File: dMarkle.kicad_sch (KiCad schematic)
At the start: 64 parts, among them SW1 SW_Choice, U1 74LS125, U10 INND-TS30RCB, U11 74LS125, U2 74HC4511, U3 Pico, U4 INND-TS30RCB, U5 74LS125, U6 74LS125, U7 74HC4511, U8 74HC4511, U9 INND-TS30RCB

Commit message: Rev 0.1
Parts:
- removed C11, C13, C15: 1u, Capacitor_THT:CP_Radial_D5.0mm_P2.00mm, symbol Device:C_Polarized_Small
- removed C12, C14, C16: 0u1, Capacitor_THT:C_Rect_L4.0mm_W2.5mm_P2.50mm, symbol Device:C_Small
- removed U1, U5, U6: 74LS125, Package_DIP:DIP-14_W7.62mm, symbol 74xx:74LS125
- removed U10, U9: INND-TS30RCB, Display_7Segment:HDSP-A151, symbol Display_Character:HDSP-A153
- removed U7, U8: 74HC4511, Package_DIP:DIP-16_W7.62mm, symbol CustomParts:74HC4511
- added D3, D4: INND-TS30RCB, Display_7Segment:HDSP-A151, symbol Display_Character:HDSP-A153
- added Q1: 2N7000, Package_TO_SOT_THT:TO-92_Inline, symbol Transistor_FET:2N7000
- added R7: 10k, Resistor_THT:R_Axial_DIN0204_L3.6mm_D1.6mm_P5.08mm_Horizontal, symbol Device:R_Small
- added SW2: SW_EN, Button_Switch_THT:SW_CuK_OS102011MA1QN1_SPDT_Angled, symbol Switch:SW_SPDT
- added U3, U4: 74HC4511, Package_DIP:DIP-16_W7.62mm, symbol CustomParts:74HC4511
- C1, C3: footprint Capacitor_THT:CP_Radial_D5.0mm_P2.00mm -> Capacitor_THT:C_Rect_L4.0mm_W2.5mm_P2.50mm; symbol Device:C_Polarized_Small -> Device:C_Small
- C5: renamed from C6; footprint Capacitor_THT:CP_Radial_D5.0mm_P2.00mm -> Capacitor_THT:C_Rect_L4.0mm_W2.5mm_P2.50mm; symbol Device:C_Polarized_Small -> Device:C_Small
- C7: renamed from C9; footprint Capacitor_THT:CP_Radial_D5.0mm_P2.00mm -> Capacitor_THT:C_Rect_L4.0mm_W2.5mm_P2.50mm; symbol Device:C_Polarized_Small -> Device:C_Small
- renumbered C8 to C10, C17 to C11, C18 to C12, C19 to C13, C7 to C6, C10 to C8, C5 to C9, U4 to D2, R9 to R10, R8 to R11, R7 to R12, R12 to R14, R14 to R29, R11 to R8, R10 to R9, U3 to U1, U11 to U5
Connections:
- net DIG0_0 is gone; now on net D0: U1.1 (GPIO0)
- net DIG0_1 is gone; now on net D1: U1.2 (GPIO1)
- net DIG0_2 is gone; now on net D2: U1.4 (GPIO2)
- net DIG0_3 is gone; now on net D3: U1.5 (GPIO3)
- net +3.3V: now also C1.1, C2.1, C3.1, C4.1, C5.1, C6.1, C7.1, C8.1, D1.2 (A), U2.16 (VCC), U2.3 (~{LT}), Q1.2 (G), R7.1, SW2.3 (C), U3.16 (VCC), U3.3 (~{LT}), U4.16 (VCC), U4.3 (~{LT})
- net +5V: now also Q1.3 (D); no longer C1.1, C2.1, C3.1, C4.1, C5.1, C6.1, C7.1, C8.1, D1.2 (A), U2.16 (VCC), U2.3 (~{LT}), U2.4 (~{BL})
- net GND: now also D3.1 (CC), D3.6 (CC), D4.1 (CC), D4.6 (CC), Q1.1 (S), R7.2, SW2.1 (A), U3.8 (GND), U4.8 (GND); no longer U2.5 (~{LE})
- net D1: now reaches U2.1 (D1)
- net D1: now also U3.1 (D1), U4.1 (D1)
- net D2: now reaches U2.2 (D2)
- net D2: now also U3.2 (D2), U4.2 (D2)
- net D3: now reaches U2.6 (D3)
- net D3: now also U3.6 (D3), U4.6 (D3)
- net D0: now reaches U2.7 (D0)
- net D0: now also U3.7 (D0), U4.7 (D0)
- net ENABLE: now reaches U1.37 (3V3_EN)
- net ENABLE: now also SW2.2 (B)
- net ~{BL}1: now reaches U1.6 (GPIO4)
- net ~{BL}1: now also U2.4 (~{BL})
- net ~{BL}2: now reaches U1.7 (GPIO5)
- net ~{BL}2: now also U3.4 (~{BL})
- net D1A: no longer names the net of R12.1, U2.13 (a)
- net D1Ar: no longer names the net of D2.10 (A), R12.2
- net D1B: no longer names the net of R11.1, U2.12 (b)
- net D1Br: no longer names the net of D2.9 (B), R11.2
- net D1C: no longer names the net of R10.1, U2.11 (c)
- net D1Cr: no longer names the net of D2.8 (C), R10.2
- net D1D: no longer names the net of R9.1, U2.10 (d)
- net D1Dr: no longer names the net of D2.5 (D), R9.2
- net D1E: no longer names the net of R8.1, U2.9 (e)
- net D1Er: no longer names the net of D2.4 (E), R8.2
- net D1F: no longer names the net of R14.1, U2.15 (f)
- net D1Fr: no longer names the net of D2.2 (F), R14.2
- net D1G: no longer names the net of R13.1, U2.14 (g)
- net D1Gr: no longer names the net of D2.3 (G), R13.2
- net D2A: no longer names the net of R15.1
- net D2A: now also U3.9 (e)
- net D2Ar: no longer names the net of R15.2
- net D2Ar: now also D3.4 (E)
- net D2B: no longer names the net of R16.1
- net D2B: now also U3.10 (d)
- net D2Br: no longer names the net of R16.2
- net D2Br: now also D3.5 (D)
- net D2C: no longer names the net of R17.1
- net D2C: now also U3.11 (c)
- net D2Cr: no longer names the net of R17.2
- net D2Cr: now also D3.8 (C)
- net D2D: no longer names the net of R18.1
- net D2D: now also U3.12 (b)
- net D2Dr: no longer names the net of R18.2
- net D2Dr: now also D3.9 (B)
- net D2E: no longer names the net of R19.1
- net D2E: now also U3.13 (a)
- net D2Er: no longer names the net of R19.2
- net D2Er: now also D3.10 (A)
- net D2F: no longer names the net of R20.1
- net D2F: now also U3.14 (g)
- net D2Fr: no longer names the net of R20.2
- net D2Fr: now also D3.3 (G)
- net D2G: no longer names the net of R21.1
- net D2G: now also U3.15 (f)
- net D2Gr: no longer names the net of R21.2
- net D2Gr: now also D3.2 (F)
- net D3A: no longer names the net of R22.1
- net D3A: now also U4.9 (e)
- net D3Ar: no longer names the net of R22.2
- net D3Ar: now also D4.4 (E)
- net D3B: no longer names the net of R23.1
- net D3B: now also U4.10 (d)
- net D3Br: no longer names the net of R23.2
- net D3Br: now also D4.5 (D)
- net D3C: no longer names the net of R24.1
- net D3C: now also U4.11 (c)
- net D3Cr: no longer names the net of R24.2
- net D3Cr: now also D4.8 (C)
- net D3D: no longer names the net of R25.1
- net D3D: now also U4.12 (b)
- net D3Dr: no longer names the net of R25.2
- net D3Dr: now also D4.9 (B)
- net D3E: no longer names the net of R26.1
- net D3E: now also U4.13 (a)
- net D3Er: no longer names the net of R26.2
- net D3Er: now also D4.10 (A)
- net D3F: no longer names the net of R27.1
- net D3F: now also U4.14 (g)
- net D3Fr: no longer names the net of R27.2
- net D3Fr: now also D4.3 (G)
- net D3G: no longer names the net of R28.1
- net D3G: now also U4.15 (f)
- net D3Gr: no longer names the net of R28.2
- net D3Gr: now also D4.2 (F)
- net DIG1_0 renamed ~{BL}3
- net ~{BL}3: now also U4.4 (~{BL})
- net DIG1_1 renamed ~{LE}1
- net ~{LE}1: now also U2.5 (~{LE})
- net DIG1_2 renamed ~{LE}2
- net ~{LE}2: now also U3.5 (~{LE})
- net DIG1_3 renamed ~{LE}3
- net ~{LE}3: now also U4.5 (~{LE})
- net DIG2_0: no longer names the net of U1.14 (GPIO10)
- net DIG2_1: no longer names the net of U1.15 (GPIO11)
- net DIG2_2: no longer names the net of U1.16 (GPIO12)
- net DIG2_3: no longer names the net of U1.17 (GPIO13)
- no-connect marks 22 -> 23
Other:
- note removed: "3V3 to 5V BCD 7-Segment Display Logic"
- moved on the sheet: C10, C11, C9, D2, R1, R10, R11, R12, R13, R14, R2, R3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

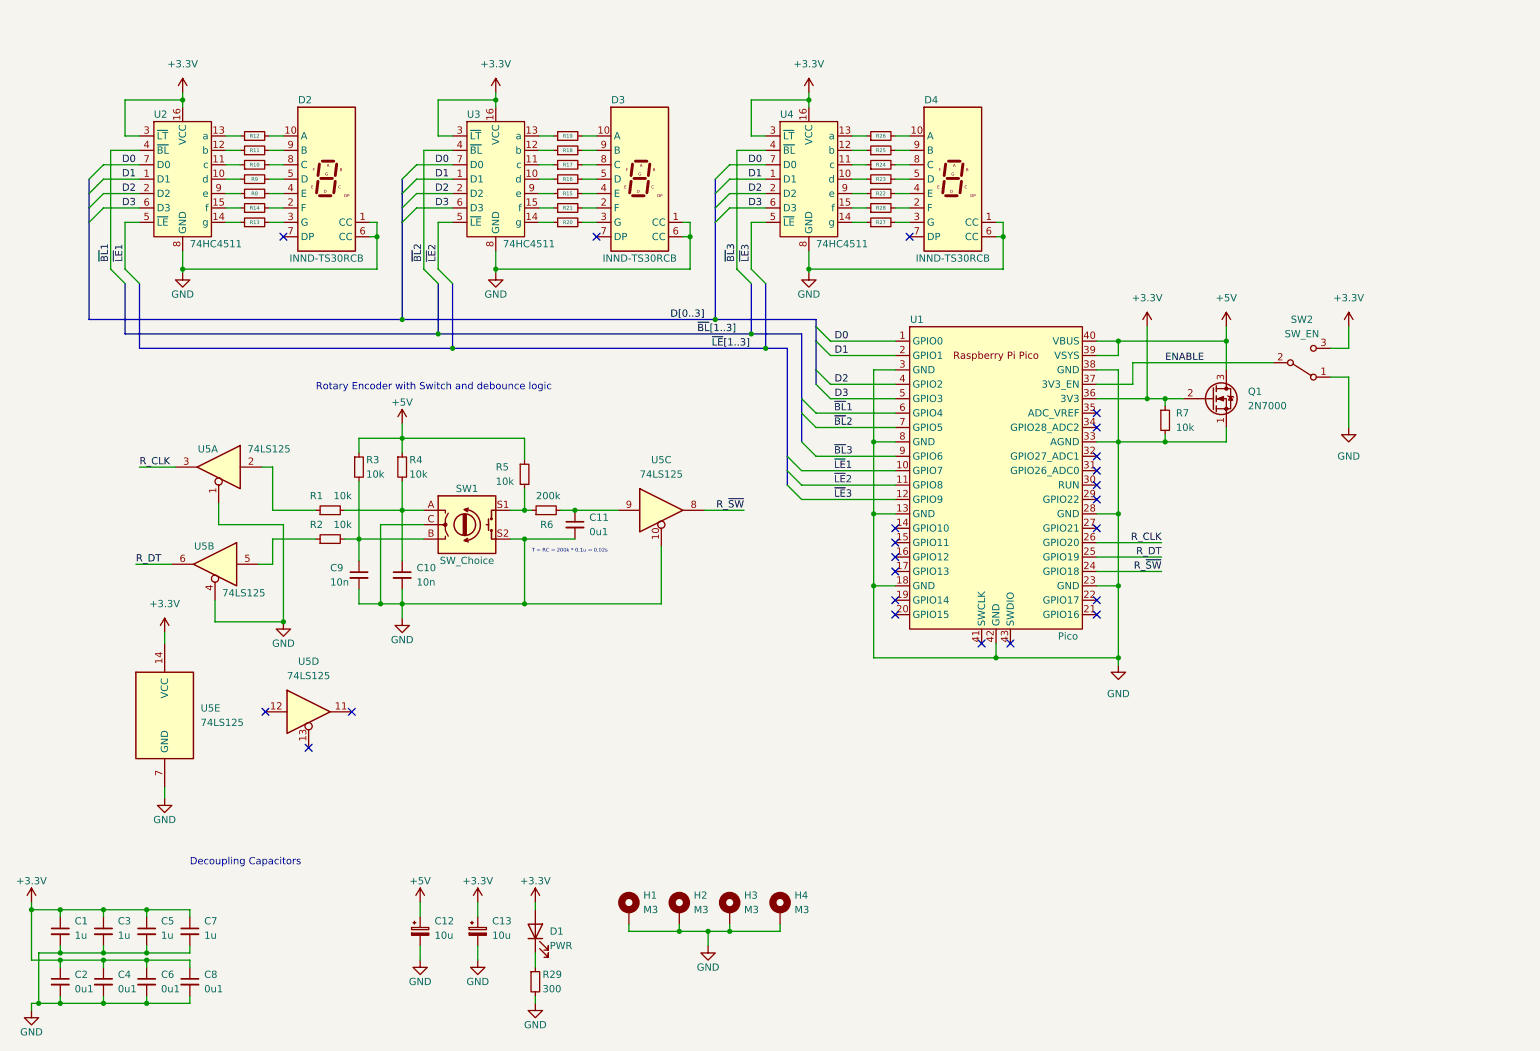
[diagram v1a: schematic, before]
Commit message: All 5V usage removed. Rev0.1 complete.
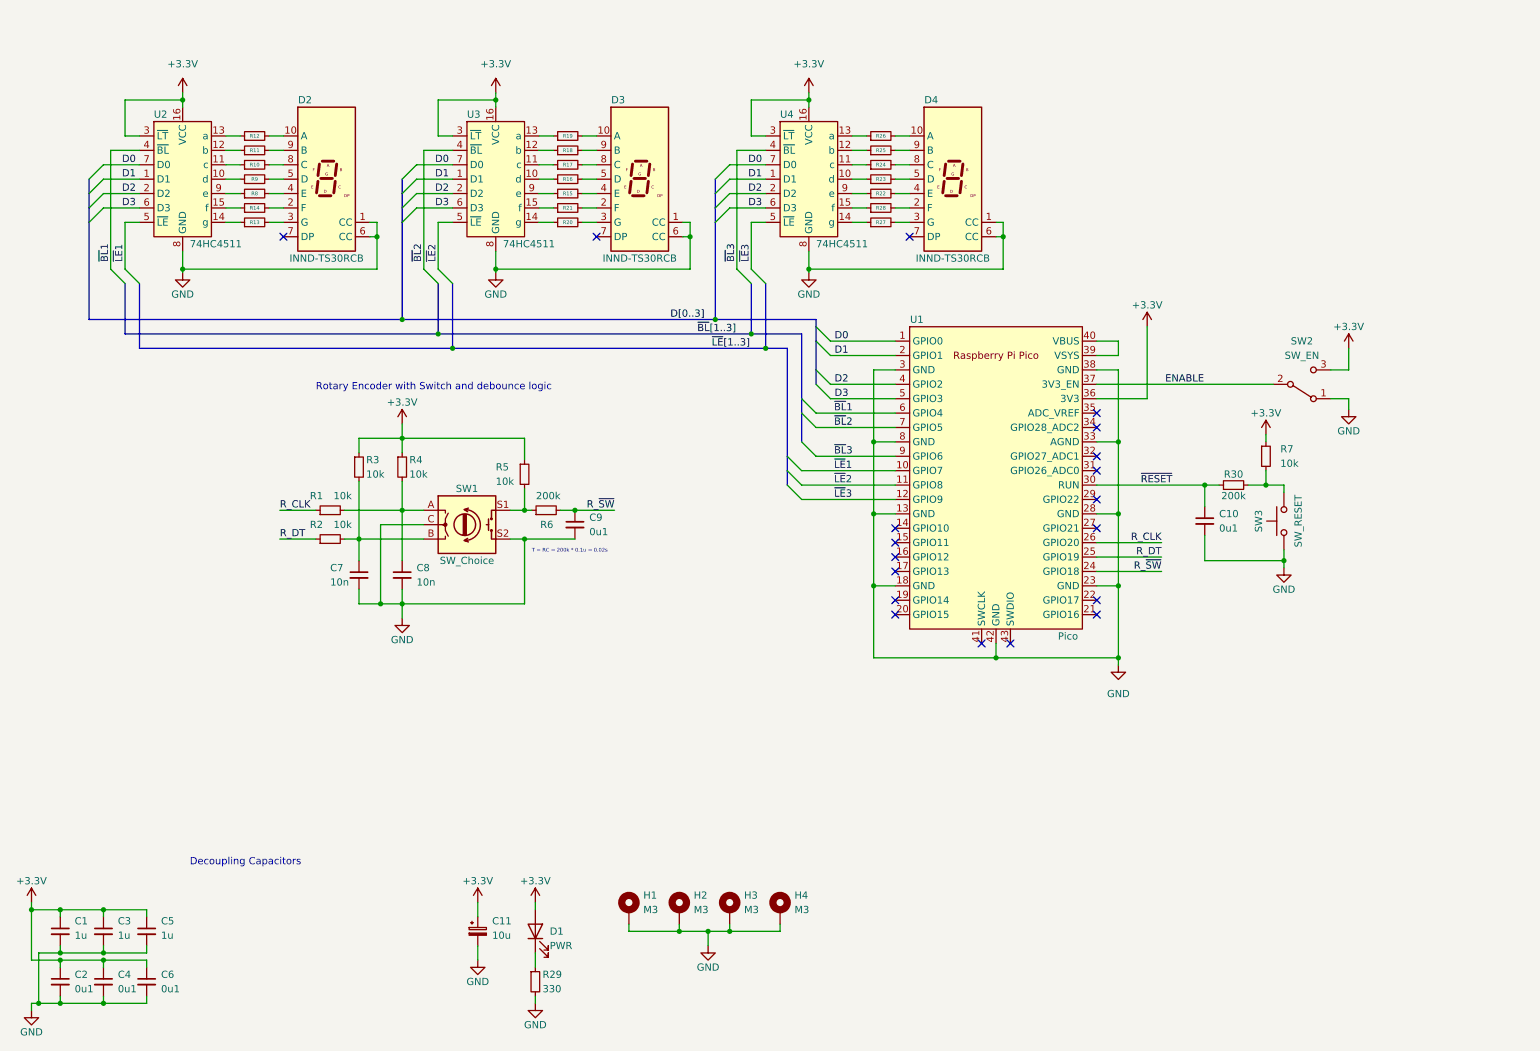
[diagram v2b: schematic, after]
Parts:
- removed C12: 10u, Capacitor_THT:CP_Radial_D5.0mm_P2.00mm, symbol Device:C_Polarized_Small
- removed C7: 1u, Capacitor_THT:C_Rect_L4.0mm_W2.5mm_P2.50mm, symbol Device:C_Small
- removed C8: 0u1, Capacitor_THT:C_Rect_L4.0mm_W2.5mm_P2.50mm, symbol Device:C_Small
- removed Q1: 2N7000, Package_TO_SOT_THT:TO-92_Inline, symbol Transistor_FET:2N7000
- removed U5: 74LS125, Package_DIP:DIP-14_W7.62mm, symbol 74xx:74LS125
- added C10: 0u1, Capacitor_THT:C_Rect_L4.0mm_W2.5mm_P2.50mm, symbol Device:C_Small
- added R30: 200k, Resistor_THT:R_Axial_DIN0204_L3.6mm_D1.6mm_P5.08mm_Horizontal, symbol Device:R_Small
- added SW3: SW_RESET, Button_Switch_THT:SW_PUSH_6mm, symbol Switch:SW_Push
- R29: value 300 -> 330
- renumbered C13 to C11, C9 to C7, C10 to C8, C11 to C9
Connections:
- net +3.3V: now also R3.1, R4.1, R5.1
- net GND: now also C10.2, SW3.1; no longer R7.2
- net R_CLK: now also R1.1
- net R_DT: now also R2.1
- net R_~{SW}: now also C9.1, R6.2
- net ~{RESET}: now reaches U1.30 (RUN)
- net ~{RESET}: now also C10.1, R30.1
- removed net +5V: R3.1, R4.1, R5.1, U1.39 (VSYS), U1.40 (VBUS)
- new net: R30.2, R7.2, SW3.2
- new net: U1.39 (VSYS), U1.40 (VBUS)
- no-connect marks 23 -> 19
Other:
- moved on the sheet: SW2

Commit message: Clean up schematic and generate output for rev 0.1
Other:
- note added: "7-Segment BCD Display"
- note added: "Mounting Holes"
- note added: "Power & Reset Switch, Power LED"
- note added: "Rotary Encoder with Switch & Debounce Circuit"
- note removed: "Rotary Encoder with Switch and debounce logic"
- moved on the sheet: C1, C10, C11, C2, C3, C4, C5, C6, C7, C8, C9, D1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

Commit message: Board and parts ordered.
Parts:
- C1, C3, C5: Manufacturer (none) -> TDK Corporation; Manufacturer Part Number (none) -> FG18X5R1H105KRT06; Supplier Part Number (none) -> 445-173257-1-ND
- C10, C2, C4, C6, C9: Manufacturer (none) -> Vishay Beyschlag/Draloric/BC Components; Manufacturer Part Number (none) -> K104K15X7RF5TL2; Supplier Part Number (none) -> BC1084CT-ND
- C11: Manufacturer (none) -> Rubycon; Manufacturer Part Number (none) -> 50YXM10MEFRTA5X11; Supplier Part Number (none) -> 1189-50YXM10MEFRTA5X11CT-ND
- C7, C8: Manufacturer (none) -> Vishay Beyschlag/Draloric/BC Components; Manufacturer Part Number (none) -> K103K15X7RF5TL2; Supplier Part Number (none) -> BC1078CT-ND
- D1: Manufacturer (none) -> Würth Elektronik; Manufacturer Part Number (none) -> 151031SS04000; Supplier Part Number (none) -> 732-5005-ND
- D2, D3, D4: Manufacturer (none) -> Inolux; Manufacturer Part Number (none) -> INND-TS30RCB; Supplier Part Number (none) -> 1830-1149-ND
- R1, R2, R3, R4, R5, R7: Manufacturer (none) -> Vishay Beyschlag/Draloric/BC Components; Manufacturer Part Number (none) -> MBA02040C1002FRP00; Supplier Part Number (none) -> BC10.0KXCT-ND
- R10, R11, R12, R13, R14, R15, R16, R17, R18, R19, R20, R21, R22, R23, R24, R25, R26, R27, R28, R29, R8, R9: Manufacturer (none) -> Vishay Beyschlag/Draloric/BC Components; Manufacturer Part Number (none) -> MBA02040C3300FCT00; Supplier Part Number (none) -> BC3292CT-ND
- R30, R6: Manufacturer (none) -> Vishay Beyschlag/Draloric/BC Components; Manufacturer Part Number (none) -> MBA02040C2003FCT00; Supplier Part Number (none) -> BC3256CT-ND
- SW2: Manufacturer (none) -> C&K; Manufacturer Part Number (none) -> OS102011MA1QN1; Supplier Part Number (none) -> CKN9559-ND
- SW3: Manufacturer (none) -> E-Switch; Manufacturer Part Number (none) -> TL1105F160Q; Supplier Part Number (none) -> EG1827-ND
- U1: Manufacturer (none) -> Raspberry Pi; Manufacturer Part Number (none) -> SC0917; Supplier Part Number (none) -> 2648-SC0917-ND
- U2, U3, U4: Manufacturer (none) -> Texas Instruments; Manufacturer Part Number (none) -> CD74HC4511E; Supplier Part Number (none) -> 296-14537-5-ND
